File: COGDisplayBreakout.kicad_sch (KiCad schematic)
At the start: 12 parts, among them J1 SPI_Header

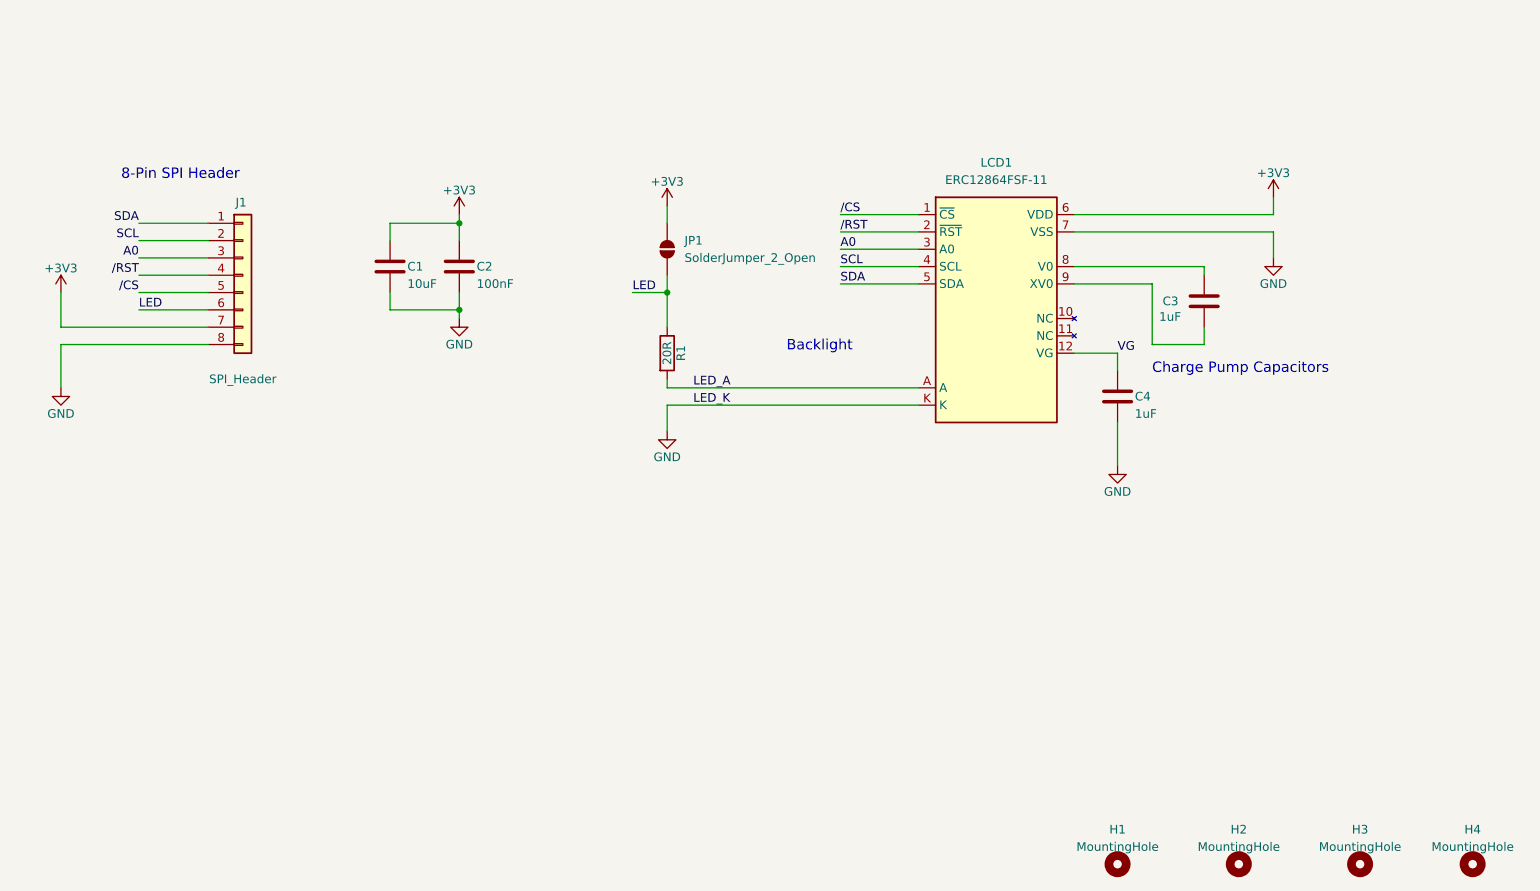
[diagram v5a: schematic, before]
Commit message: Adds power on reset
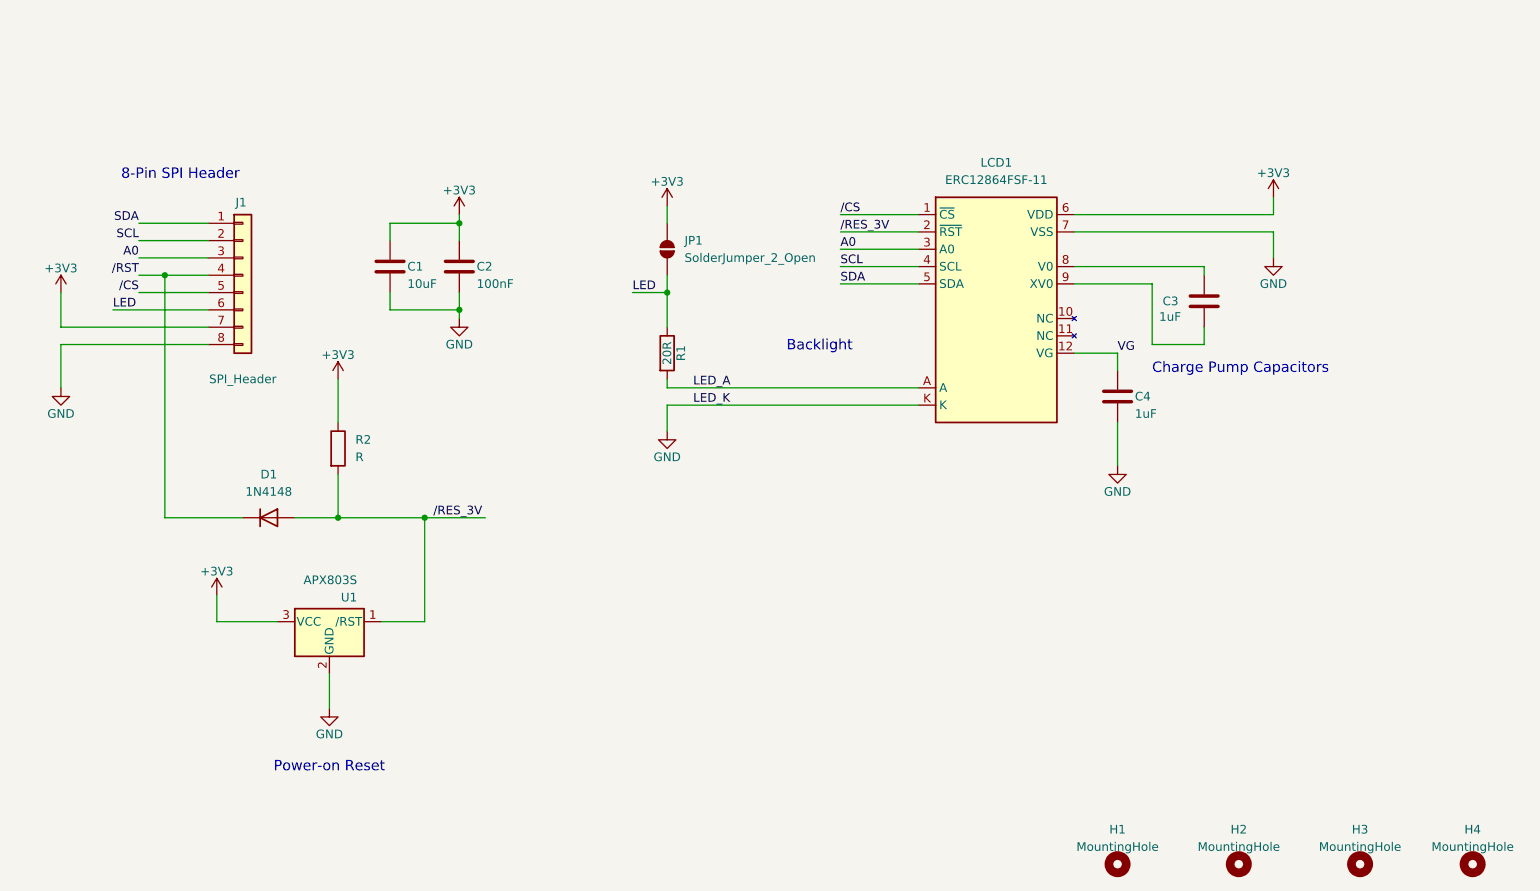
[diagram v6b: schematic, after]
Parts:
- added D1: 1N4148, Diode_SMD:D_0805_2012Metric_Pad1.15x1.40mm_HandSolder, symbol Diode:1N4148
- added R2: R, Resistor_SMD:R_0805_2012Metric_Pad1.20x1.40mm_HandSolder, symbol Device:R
- added U1: APX803S, Package_TO_SOT_SMD:TSOT-23, symbol Power_Management:APX803S
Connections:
- net +3V3: now also R2.1, U1.3 (VCC)
- net /RST: now also D1.1 (K); no longer LCD1.2 (~{RST})
- net GND: now also U1.2 (GND)
- new net /RES_3V: D1.2 (A), LCD1.2 (~{RST}), R2.2, U1.1 (/RST)
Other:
- note added: "Power-on Reset"
